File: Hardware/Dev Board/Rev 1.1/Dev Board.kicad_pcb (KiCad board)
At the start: 2 copper layers, 100 x 100 mm, 43 parts, among them J1 VBAT, J2 RJ45_LED, J3 GPIO, J4 Ethernet, J5 USB_C_Receptacle_USB2.0, J6 6502 Bus, J7 USB Host, J8 Panel, J9 Serial, SW1 Run/Stop, SW2 Step, SW3 Clock, SW4 Reset, U1 TXS0108EPW, U2 TXS0108EPW, U3 Teensy4.1, U4 TXS0108EPW, U5 TXS0108EPW

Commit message: Better 3D models and images
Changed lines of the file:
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@@
 		(model "${KIPRJMOD}/../../../CAD/61204021621.step"
 			(offset
-				(xyz 1.25 -23.5 4.5)
+				(xyz 1.25 -24 4.5)
 			)
 			(scale
@@
 		)
 		(property "Value" "Teensy4.1"
-			(at -1.7 0 0)
+			(at -8.9 0.2 0)
 			(layer "F.SilkS")
 			(effects
@@
 			(layer "F.SilkS")
 		)
+		(fp_text user "Ethernet"
+			(at -12.065 -3.2766 180)
+			(layer "F.SilkS")
+			(effects
+				(font
+					(size 1 1)
+					(thickness 0.15)
+				)
+			)
+		)
+		(fp_text user "Micro SD"
+			(at 24.13 0 90)
+			(layer "F.SilkS")
+			(effects
+				(font
+					(size 1 1)
+					(thickness 0.15)
+				)
+			)
+		)
+		(fp_text user "USB Host"
+			(at -18.4658 2.4892 90)
+			(layer "F.SilkS")
+			(effects
+				(font
+					(size 1 1)
+					(thickness 0.15)
+				)
+			)
+		)
+		(fp_text user "DVJ6A"
+			(at -2.54 -0.18 0)
+			(layer "F.SilkS")
+			(effects
+				(font
+					(size 0.7 0.7)
+					(thickness 0.15)
+				)
+			)
+		)
+		(fp_text user "MIMXRT1062"
+			(at -1.27 0 0)
+			(layer "F.SilkS")
+			(effects
+				(font
+					(size 0.7 0.7)
+					(thickness 0.15)
+				)
+			)
+		)
+		(fp_text user "USB"
+			(at -26.67 0 0)
+			(layer "F.SilkS")
+			(effects
+				(font
+					(size 1 1)
+					(thickness 0.15)
+				)
+			)
+		)
 		(pad "1" thru_hole rect
 			(at -29.21 7.62 90)
@@
 		(model "${KIPRJMOD}/../../../CAD/Teensy_4.1_Assembly.step"
 			(offset
-				(xyz 0 0 0.762)
+				(xyz 0 0 11)
 			)
 			(scale
@@
 			)
 			(rotate
-				(xyz 0 0 0)
-			)
-		)
+				(xyz -0 -0 -0)
+			)
+		)
+		(model "${KICAD9_3DMODEL_DIR}/Connector_PinHeader_2.54mm.3dshapes/PinHeader_1x24_P2.54mm_Vertical.step"
+			(offset
+				(xyz -29 7.5 11)
+			)
+			(scale
+				(xyz 1 1 1)
+			)
+			(rotate
+				(xyz -0 -180 -90)
+			)
+		)
+		(model "${KICAD9_3DMODEL_DIR}/Connector_PinHeader_2.54mm.3dshapes/PinHeader_1x24_P2.54mm_Vertical.step"
+			(offset
+				(xyz -29 -7.5 11)
+			)
+			(scale
+				(xyz 1 1 1)
+			)
+			(rotate
+				(xyz -0 -180 -90)
+			)
+		)
+		(model "${KICAD9_3DMODEL_DIR}/Connector_PinHeader_2.54mm.3dshapes/PinHeader_1x05_P2.54mm_Vertical.step"
+			(offset
+				(xyz 16.5 5 11)
+			)
+			(scale
+				(xyz 1 1 1)
+			)
+			(rotate
+				(xyz -0 -180 -0)
+			)
+		)
+		(model "${KICAD9_3DMODEL_DIR}/Connector_PinHeader_2.54mm.3dshapes/PinHeader_1x05_P2.54mm_Vertical.step"
+			(offset
+				(xyz -23 -4.5 11)
+			)
+			(scale
+				(xyz 1 1 1)
+			)
+			(rotate
+				(xyz -0 -180 -90)
+			)
+		)
+		(model "${KICAD9_3DMODEL_DIR}/Connector_PinHeader_2.00mm.3dshapes/PinHeader_2x03_P2.00mm_Vertical.step"
+			(offset
+				(xyz -14.25 5 11)
+			)
+			(scale
+				(xyz 1 1 1)
+			)
+			(rotate
+				(xyz -0 -180 -0)
+			)
+		)
+		(model "${KICAD9_3DMODEL_DIR}/Connector_PinSocket_2.54mm.3dshapes/PinSocket_1x24_P2.54mm_Vertical.step"
+			(offset
+				(xyz -29 -7.5 0)
+			)
+			(scale
+				(xyz 1 1 1)
+			)
+			(rotate
+				(xyz -0 -0 -90)
+			)
+		)
+		(model "${KICAD9_3DMODEL_DIR}/Connector_PinSocket_2.54mm.3dshapes/PinSocket_1x24_P2.54mm_Vertical.step"
+			(offset
+				(xyz -29 7.5 0)
+			)
+			(scale
+				(xyz 1 1 1)
+			)
+			(rotate
+				(xyz -0 -0 -90)
+			)
+		)
+		(model "${KICAD9_3DMODEL_DIR}/Connector_PinSocket_2.00mm.3dshapes/PinSocket_2x03_P2.00mm_Vertical.step"
+			(offset
+				(xyz -14.25 5 0)
+			)
+			(scale
+				(xyz 1 1 1)
+			)
+			(rotate
+				(xyz -0 -0 -0)
+			)
+		)
+		(model "${KICAD9_3DMODEL_DIR}/Connector_PinSocket_2.54mm.3dshapes/PinSocket_1x05_P2.54mm_Vertical.step"
+			(offset
+				(xyz 16.5 5 0)
+			)
+			(scale
+				(xyz 1 1 1)
+			)
+			(rotate
+				(xyz -0 -0 -0)
+			)
+		)
+		(model "${KICAD9_3DMODEL_DIR}/Connector_PinSocket_2.54mm.3dshapes/PinSocket_1x05_P2.54mm_Vertical.step"
+			(offset
+				(xyz -23 -4.5 0)
+			)
+			(scale
+				(xyz 1 1 1)
+			)
+			(rotate
+				(xyz -0 -0 -90)
+			)
+		)

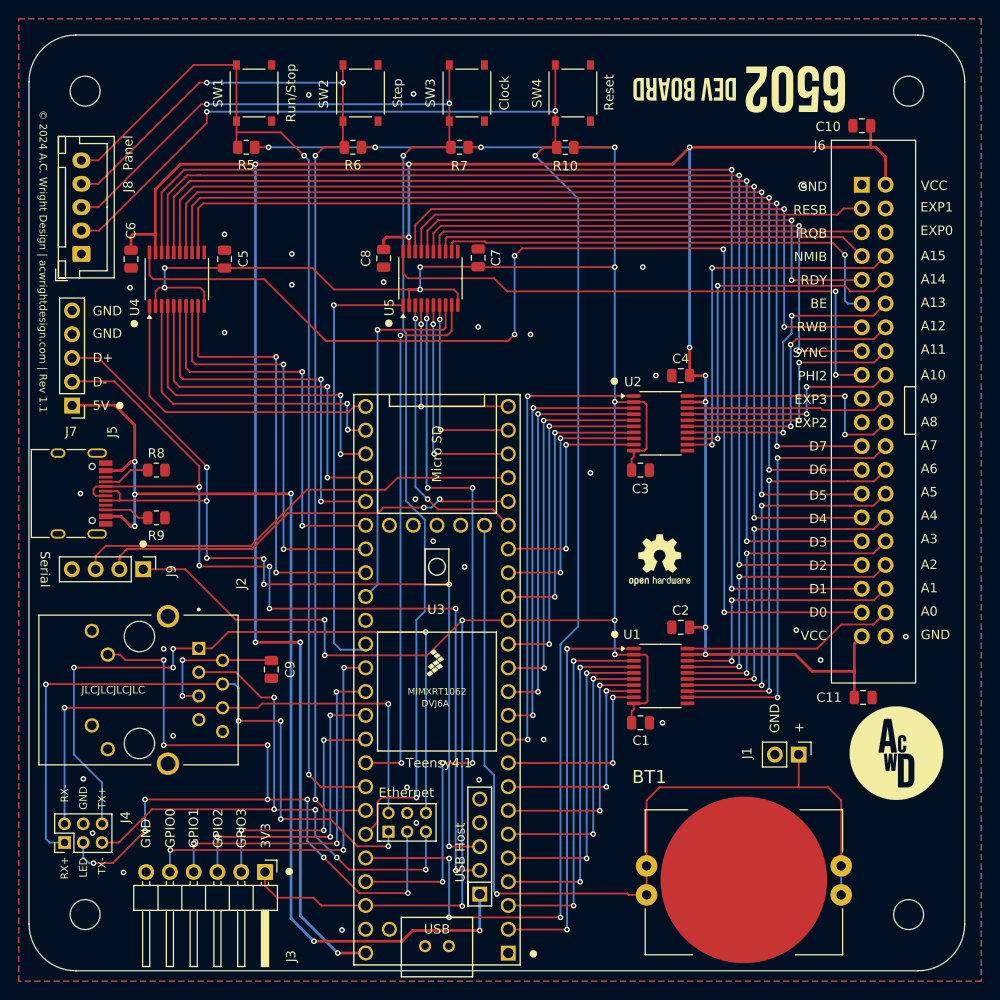
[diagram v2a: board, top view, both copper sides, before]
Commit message: Update DB 1.1 to add OE control lines
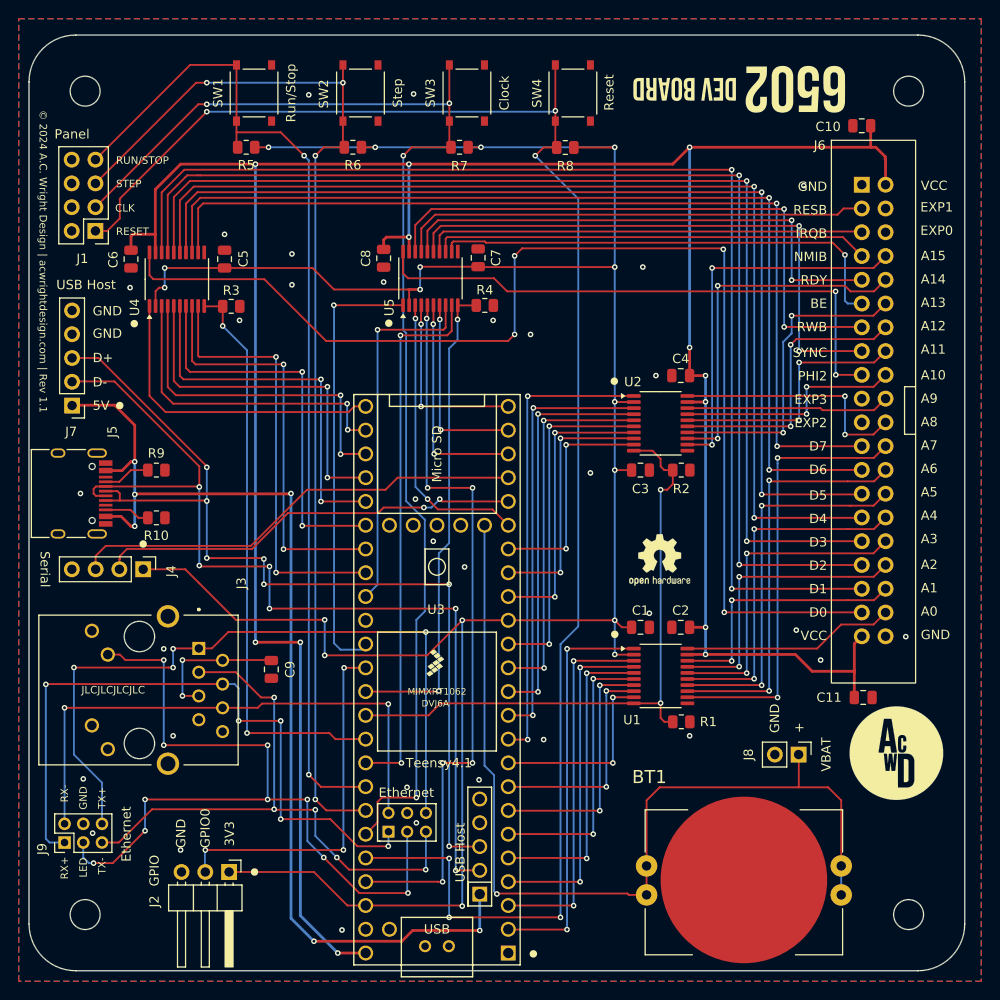
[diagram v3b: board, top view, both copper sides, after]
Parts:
- added R1: 100k, Resistor_SMD:R_0805_2012Metric, F.Cu at (159.7, 123.4)
- added R2: 100k, Resistor_SMD:R_0805_2012Metric, F.Cu at (159.7, 96.5)
- added R3: 100k, Resistor_SMD:R_0805_2012Metric, F.Cu at (111.6, 79.0)
- added R4: 100k, Resistor_SMD:R_0805_2012Metric, F.Cu at (138.7, 78.9)
- J1: renamed from J8; footprint Connector_JST:JST_XH_B5B-XH-A_1x05_P2.50mm_Vertical -> Connector_PinHeader_2.54mm:PinHeader_2x04_P2.54mm_Vertical
- J2: renamed from J3; footprint Connector_PinHeader_2.54mm:PinHeader_1x06_P2.54mm_Horizontal -> Connector_PinHeader_2.54mm:PinHeader_1x03_P2.54mm_Horizontal
- J5: value USB_C_Receptacle_USB2.0 -> USB Host
- moved C1 10.2 mm to (155.3, 113.3)
- moved J2 3.84 mm to (111.4, 139.4)
- moved J1 2.88 mm to (97.1, 70.9), turned to 180 degrees
- renumbered J2 to J3, J9 to J4, J1 to J8, J4 to J9, R9 to R10, R10 to R8, R8 to R9
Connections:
- J1 pad 1: GND -> RES_SW
- J1 pad 2: RES_SW -> GND
- J1 pad 4: STEP_SW -> GND
- J1 pad 5: RUN_STOP_SW -> STEP_SW
- J2 pad 2: GPIO_3 -> GPIO_0
- J2 pad 3: GPIO_2 -> GND
- U1 pad 10: 3V3 -> OE2_3V3
- U2 pad 10: 3V3 -> OE2_3V3
- U3 pad 37: GPIO_1 -> OE3_3V3
- U3 pad 38: GPIO_2 -> OE2_3V3
- U3 pad 39: GPIO_3 -> OE1_3V3
- U4 pad 10: 3V3 -> OE1_3V3
- U5 pad 10: 3V3 -> OE3_3V3
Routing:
- net OE2_3V3: track 0.00 -> 66.5 mm, vias 0 -> 2
- net OE1_3V3: track 0.00 -> 61.8 mm, vias 0 -> 2
- net OE3_3V3: track 0.00 -> 51.9 mm, vias 0 -> 2
- net GPIO_1: track 37.7 -> 0.00 mm, vias 3 -> 0
- net GPIO_2: track 32.7 -> 0.00 mm, vias 3 -> 0
- net GPIO_3: track 27.4 -> 0.00 mm, vias 3 -> 0
- net 3V3: track 306.4 -> 282.3 mm, vias 16 -> 17
- net GPIO_0: track 42.5 -> 38.6 mm
- net RUN_STOP_SW: track 111.0 -> 109.5 mm
- net STEP_SW: track 119.4 -> 117.9 mm
- net CLK_SW: track 136.5 -> 135.0 mm
- net RES_SW: track 179.4 -> 178.5 mm
- net GND: vias 32 -> 33
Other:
- board text added: "CLK"
- board text added: "RESET"
- board text added: "RUN/STOP"
- board text added: "STEP"
- board text removed: "GPIO1"
- board text removed: "GPIO2"
- board text removed: "GPIO3"
